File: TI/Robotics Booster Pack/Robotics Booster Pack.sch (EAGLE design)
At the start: 81 parts, among them U11 SCHA4B0400, U13 XBEE-1XBEE-1_LOCK, U14 TPS5450, U16 TPS62152.RGT, U3 DRV8800, U4 DRV8800, U5 DRV8800, U6 DRV8800, U7 PCA9557.RGV, U8 MPU-6050, U9 INA220.DGS

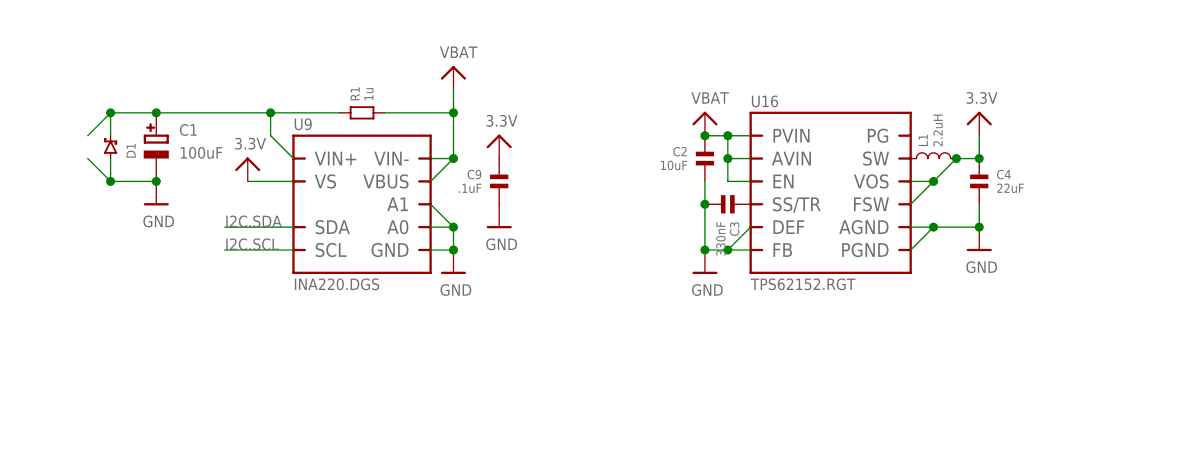
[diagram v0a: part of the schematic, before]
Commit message: Continued working on RBP v3 Using TPS62177 for 3.3v regulator circuit, new Vin headers, moving things around.
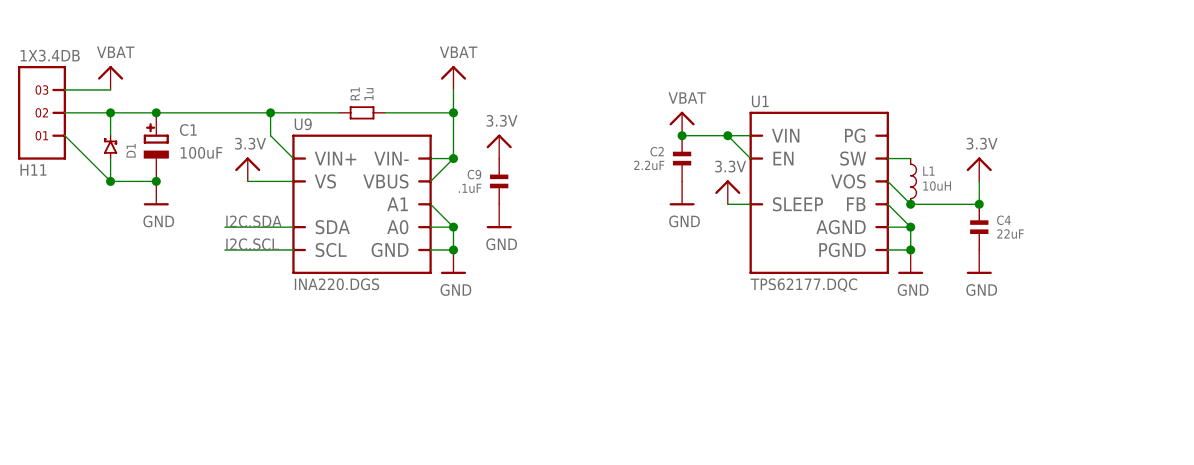
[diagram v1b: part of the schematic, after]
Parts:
- removed C3: 330nF, standardparts:CAPACITOR.0603
- removed U16: TPS62152.RGT, packages(ti):TPS6215X.RGT
- added H11: 1X3.4DB, te-connectivity:1X3.4DB
- added U1: TPS62177.DQC, packages(ti):TPS62177.DQC
- C2: value 10uF -> 2.2uF
- L1: value 2.2uH -> 10uH; device coilcraft:INDUCTOR.XAL4020 -> bourns:INDUCTOR-SRN6045
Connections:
- removed net N$23: C3.1, U16.SS/TR
- net 3.3V: now also U1.SLEEP, U1.VOS; no longer U16.FSW, U16.VOS
- net GND: now also H11.1, U1.AGND, U1.FB, U1.PGND; no longer C3.2, U16.AGND, U16.DEF, U16.FB, U16.PGND
- net N$1: now also U1.SW; no longer U16.SW
- net N$22: now also H11.2
- net VBAT: now also H11.3, U1.EN, U1.VIN; no longer U16.AVIN, U16.EN, U16.PVIN
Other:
- moved on the sheet: C2, C4, L1

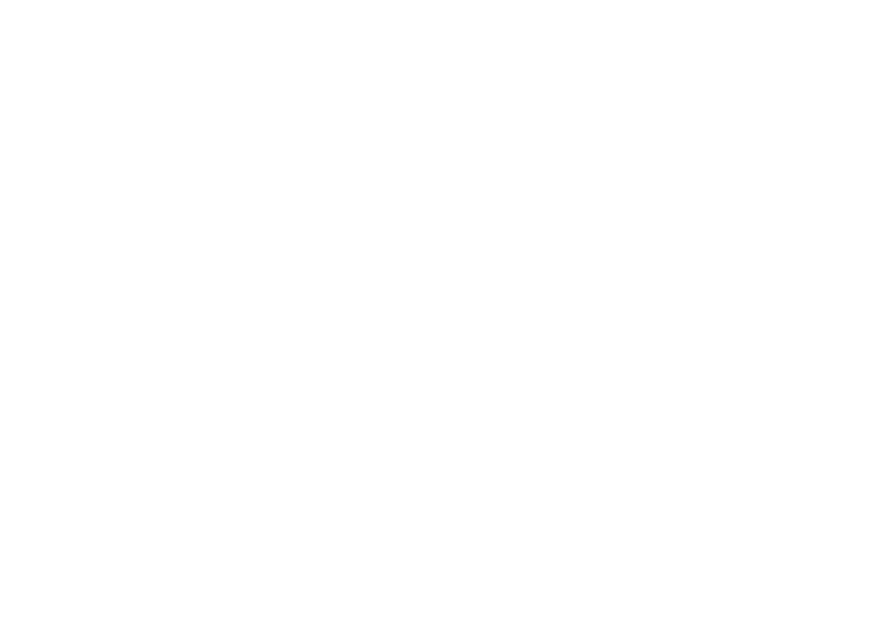
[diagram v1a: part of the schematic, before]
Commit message: COntinuing work on RBP v3 Added smd headers to replace Launchpad throguh hole headers (more routing space on the bottom) Moved around motor controllers -n- stuff.
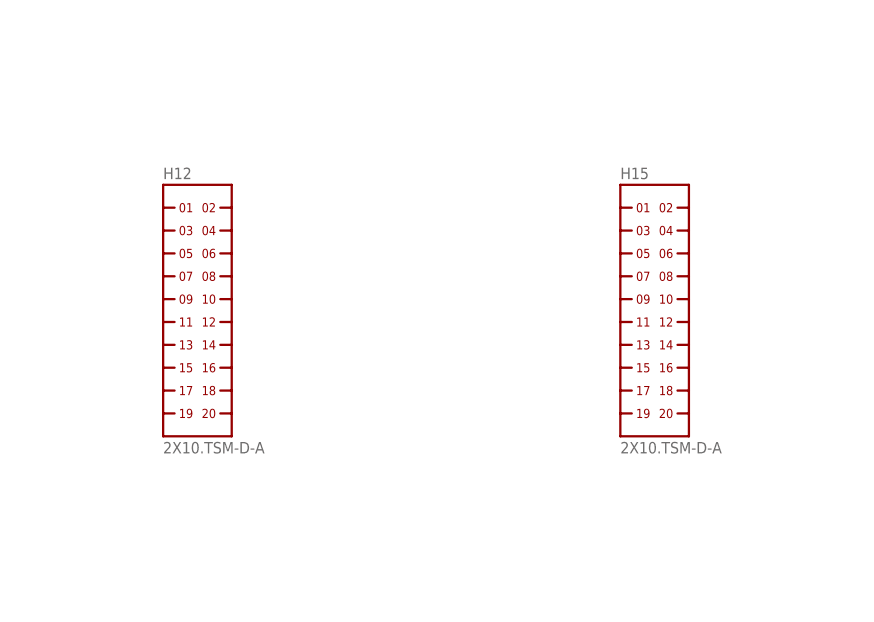
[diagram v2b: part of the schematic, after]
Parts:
- added H12, H15: 2X10.TSM-D-A, headers(.1in)(samtec):2X10.TSM-D-A
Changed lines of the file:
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@@
 <grid distance="0.1" unitdist="inch" unit="inch" style="lines" multiple="1" display="no" altdistance="0.01" altunitdist="inch" altunit="inch"/>
 <layers>
-<layer number="1" name="Top" color="4" fill="1" visible="yes" active="no"/>
-<layer number="2" name="Route2" color="1" fill="3" visible="yes" active="no"/>
-<layer number="3" name="Route3" color="4" fill="3" visible="yes" active="no"/>
-<layer number="4" name="Route4" color="1" fill="4" visible="yes" active="no"/>
-<layer number="5" name="Route5" color="4" fill="4" visible="yes" active="no"/>
-<layer number="6" name="Route6" color="1" fill="8" visible="yes" active="no"/>
-<layer number="7" name="Route7" color="4" fill="8" visible="yes" active="no"/>
-<layer number="8" name="Route8" color="1" fill="2" visible="yes" active="no"/>
-<layer number="9" name="Route9" color="4" fill="2" visible="yes" active="no"/>
-<layer number="10" name="Route10" color="1" fill="7" visible="yes" active="no"/>
-<layer number="11" name="Route11" color="4" fill="7" visible="yes" active="no"/>
-<layer number="12" name="Route12" color="1" fill="5" visible="yes" active="no"/>
-<layer number="13" name="Route13" color="4" fill="5" visible="yes" active="no"/>
-<layer number="14" name="Route14" color="1" fill="6" visible="yes" active="no"/>
-<layer number="15" name="Route15" color="4" fill="6" visible="yes" active="no"/>
-<layer number="16" name="Bottom" color="1" fill="1" visible="yes" active="no"/>
-<layer number="17" name="Pads" color="2" fill="1" visible="yes" active="no"/>
-<layer number="18" name="Vias" color="2" fill="1" visible="yes" active="no"/>
-<layer number="19" name="Unrouted" color="6" fill="1" visible="yes" active="no"/>
-<layer number="20" name="Dimension" color="15" fill="1" visible="yes" active="no"/>
-<layer number="21" name="tPlace" color="7" fill="1" visible="yes" active="no"/>
-<layer number="22" name="bPlace" color="7" fill="1" visible="yes" active="no"/>
-<layer number="23" name="tOrigins" color="15" fill="1" visible="yes" active="no"/>
-<layer number="24" name="bOrigins" color="15" fill="1" visible="yes" active="no"/>
-<layer number="25" name="tNames" color="7" fill="1" visible="yes" active="no"/>
-<layer number="26" name="bNames" color="7" fill="1" visible="yes" active="no"/>
-<layer number="27" name="tValues" color="7" fill="1" visible="yes" active="no"/>
-<layer number="28" name="bValues" color="7" fill="1" visible="yes" active="no"/>
+<layer number="1" name="Top" color="4" fill="1" visible="no" active="no"/>
+<layer number="2" name="Route2" color="1" fill="3" visible="no" active="no"/>
+<layer number="3" name="Route3" color="4" fill="3" visible="no" active="no"/>
+<layer number="4" name="Route4" color="1" fill="4" visible="no" active="no"/>
+<layer number="5" name="Route5" color="4" fill="4" visible="no" active="no"/>
+<layer number="6" name="Route6" color="1" fill="8" visible="no" active="no"/>
+<layer number="7" name="Route7" color="4" fill="8" visible="no" active="no"/>
+<layer number="8" name="Route8" color="1" fill="2" visible="no" active="no"/>
+<layer number="9" name="Route9" color="4" fill="2" visible="no" active="no"/>
+<layer number="10" name="Route10" color="1" fill="7" visible="no" active="no"/>
+<layer number="11" name="Route11" color="4" fill="7" visible="no" active="no"/>
+<layer number="12" name="Route12" color="1" fill="5" visible="no" active="no"/>
+<layer number="13" name="Route13" color="4" fill="5" visible="no" active="no"/>
+<layer number="14" name="Route14" color="1" fill="6" visible="no" active="no"/>
+<layer number="15" name="Route15" color="4" fill="6" visible="no" active="no"/>
+<layer number="16" name="Bottom" color="1" fill="1" visible="no" active="no"/>
+<layer number="17" name="Pads" color="2" fill="1" visible="no" active="no"/>
+<layer number="18" name="Vias" color="2" fill="1" visible="no" active="no"/>
+<layer number="19" name="Unrouted" color="6" fill="1" visible="no" active="no"/>
+<layer number="20" name="Dimension" color="15" fill="1" visible="no" active="no"/>
+<layer number="21" name="tPlace" color="7" fill="1" visible="no" active="no"/>
+<layer number="22" name="bPlace" color="7" fill="1" visible="no" active="no"/>
+<layer number="23" name="tOrigins" color="15" fill="1" visible="no" active="no"/>
+<layer number="24" name="bOrigins" color="15" fill="1" visible="no" active="no"/>
+<layer number="25" name="tNames" color="7" fill="1" visible="no" active="no"/>
+<layer number="26" name="bNames" color="7" fill="1" visible="no" active="no"/>
+<layer number="27" name="tValues" color="7" fill="1" visible="no" active="no"/>
+<layer number="28" name="bValues" color="7" fill="1" visible="no" active="no"/>
 <layer number="29" name="tStop" color="7" fill="3" visible="no" active="no"/>
 <layer number="30" name="bStop" color="7" fill="6" visible="no" active="no"/>
@@
 <layer number="35" name="tGlue" color="7" fill="4" visible="no" active="no"/>
 <layer number="36" name="bGlue" color="7" fill="5" visible="no" active="no"/>
-<layer number="37" name="tTest" color="7" fill="1" visible="yes" active="no"/>
-<layer number="38" name="bTest" color="7" fill="1" visible="yes" active="no"/>
+<layer number="37" name="tTest" color="7" fill="1" visible="no" active="no"/>
+<layer number="38" name="bTest" color="7" fill="1" visible="no" active="no"/>
 <layer number="39" name="tKeepout" color="4" fill="11" visible="no" active="no"/>
 <layer number="40" name="bKeepout" color="1" fill="11" visible="no" active="no"/>
@@
 <layer number="44" name="Drills" color="7" fill="1" visible="no" active="no"/>
 <layer number="45" name="Holes" color="7" fill="1" visible="no" active="no"/>
-<layer number="46" name="Milling" color="3" fill="1" visible="yes" active="no"/>
-<layer number="47" name="Measures" color="7" fill="1" visible="yes" active="no"/>
-<layer number="48" name="Document" color="7" fill="1" visible="yes" active="no"/>
-<layer number="49" name="Reference" color="7" fill="1" visible="yes" active="no"/>
-<layer number="50" name="dxf" color="7" fill="1" visible="yes" active="no"/>
-<layer number="51" name="tDocu" color="7" fill="1" visible="yes" active="no"/>
-<layer number="52" name="bDocu" color="7" fill="1" visible="yes" active="no"/>
-<layer number="53" name="tGND_GNDA" color="7" fill="9" visible="yes" active="no"/>
-<layer number="54" name="bGND_GNDA" color="1" fill="9" visible="yes" active="no"/>
-<layer number="56" name="wert" color="7" fill="1" visible="yes" active="no"/>
-<layer number="59" name="tCarbon" color="7" fill="1" visible="yes" active="no"/>
-<layer number="60" name="bCarbon" color="7" fill="1" visible="yes" active="no"/>
+<layer number="46" name="Milling" color="3" fill="1" visible="no" active="no"/>
+<layer number="47" name="Measures" color="7" fill="1" visible="no" active="no"/>
+<layer number="48" name="Document" color="7" fill="1" visible="no" active="no"/>
+<layer number="49" name="Reference" color="7" fill="1" visible="no" active="no"/>
+<layer number="50" name="dxf" color="7" fill="1" visible="no" active="no"/>
+<layer number="51" name="tDocu" color="7" fill="1" visible="no" active="no"/>
+<layer number="52" name="bDocu" color="7" fill="1" visible="no" active="no"/>
+<layer number="53" name="tGND_GNDA" color="7" fill="9" visible="no" active="no"/>
+<layer number="54" name="bGND_GNDA" color="1" fill="9" visible="no" active="no"/>
+<layer number="56" name="wert" color="7" fill="1" visible="no" active="no"/>
+<layer number="59" name="tCarbon" color="7" fill="1" visible="no" active="no"/>
+<layer number="60" name="bCarbon" color="7" fill="1" visible="no" active="no"/>
 <layer number="91" name="Nets" color="2" fill="1" visible="yes" active="yes"/>
 <layer number="92" name="Busses" color="1" fill="1" visible="yes" active="yes"/>
@@
 <part name="L1" library="bourns" deviceset="INDUCTOR" device="-SRN6045" value="10uH"/>
 <part name="U$15" library="microbuilder" deviceset="3.3V" device=""/>
+<part name="H12" library="headers(.1in)(samtec)" deviceset="2X10" device=".TSM-D-A"/>
+<part name="H15" library="headers(.1in)(samtec)" deviceset="2X10" device=".TSM-D-A"/>
 </parts>
 <sheets>
@@
 <instance part="L1" gate="G$1" x="104.14" y="231.14" rot="R270"/>
 <instance part="U$15" gate="G$1" x="83.82" y="231.14"/>
+<instance part="H12" gate="G$1" x="307.34" y="154.94"/>
+<instance part="H15" gate="G$1" x="358.14" y="154.94"/>
 </instances>
 <busses>

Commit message: Continuing RBP v3 rerouting. Figured out desired placement of headers. Thinking of adding FET to control power going out of board (NTMFS4897NFT1G). Need to replace IO expander; might need 16 pins instead of 8. Already running low on space...
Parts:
- removed C34: 100uF, microbuilder:CAP_ELECTROLYTICPANASONIC_D
- removed C39: 220uF, microbuilder:CAP_ELECTROLYTICPANASONIC_D
- removed H13, H14: 2X3, headers(.1in):2X3
- added H16, H17, H18, H19, H20, H21, H22, H23, H25, H26, H27, H28: 1X4, headers(.1in):1X4
- H1, H2, H3, H4, H5, H6: value 1X6 -> 1X4; device headers(.1in):1X6 -> headers(.1in):1X4
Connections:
- removed net VSERVO: C39.+, H2.1, H2.2, H2.3, H2.4, H2.5, H2.6
- new net N$12: H12.9
- new net N$15: H12.11
- new net N$16: H12.13
- new net N$17: H12.15
- new net N$2: H12.1
- new net N$23: H12.17
- new net N$26: H12.19
- new net N$28: H12.20
- new net N$3: H12.3
- new net N$30: H12.18
- new net N$31: H12.16
- new net N$32: H12.14
- new net N$36: H12.12
- new net N$41: H12.10
- new net N$42: H12.8
- new net N$43: H12.6
- new net N$44: H12.4
- new net N$45: H12.2
- new net N$46: H15.1
- new net N$47: H15.3
- new net N$48: H15.5
- new net N$49: H15.7
- new net N$50: H15.9
- new net N$51: H15.11
- new net N$52: H15.13
- new net N$53: H15.15
- new net N$54: H15.17
- new net N$55: H15.19
- new net N$56: H15.20
- new net N$57: H15.18
- new net N$58: H15.16
- new net N$59: H15.14
- new net N$6: H12.7
- new net N$60: H15.12
- new net N$61: H15.10
- new net N$62: H15.8
- new net N$63: H15.6
- new net N$64: H15.4
- new net N$65: H15.2
- new net N$66: H20.1, H20.2, H20.3, H20.4
- new net N$67: H23.1, H23.2, H23.3, H23.4
- new net N$68: H27.1, H27.2, H27.3, H27.4
- new net N$69: H2.1, H2.2, H2.3, H2.4
- new net N$70: H5.1, H5.2, H5.3, H5.4
- new net N$71: H17.1, H17.2, H17.3, H17.4
- net 3.3V: no longer H13.3, H14.3
- net AD0: no longer H6.1
- net AD1: no longer H6.2
- net AD2: no longer H6.3
- net AD3: no longer H6.4
- net AD4: no longer H6.5
- net AD5: no longer H6.6
- net GND: now also H11.3, H18.1, H18.2, H18.3, H18.4, H21.1, H21.2, H21.3, H21.4, H25.1, H25.2, H25.3, H25.4, H28.1, H28.2, H28.3, H28.4, H3.1, H3.2, H3.3, H3.4, H6.1, H6.2, H6.3, H6.4; no longer C34.-, C39.-, H1.1, H1.2, H1.3, H1.4, H1.5, H1.6, H11.1, H13.1, H14.1, H4.1, H4.2, H4.3, H4.4, H4.5, H4.6
- net N$4: now also H12.5; no longer C34.+, H5.1, H5.2, H5.3, H5.4, H5.5, H5.6
- net QEI0.A: no longer H13.5
- net QEI0.B: no longer H13.6
- net QEI1.A: no longer H14.5
- net QEI1.B: no longer H14.6
- net SVRO0: no longer H3.1
- net SVRO1: no longer H3.2
- net SVRO2: no longer H3.3
- net SVRO3: no longer H3.4
- net SVRO4: no longer H3.5
- net SVRO5: no longer H3.6
- net VBAT: now also H11.1; no longer H11.3
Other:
- note added: "TODO: - Move Launchpad pinouts to SMD headers - - Add UART1, I2C0, and SSI0 headers -"
- moved on the sheet: H11

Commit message: Got everything mostly figured out as to where I want things. Using larger capacitors. Pin header mappings decided on. Routing will be hell... Still need to figure out how to distribute all power variants (3.3, 5v, Vin) to all header blocks (3.3v for signals, 5v for signals/servos, Vin for servo overvolting)
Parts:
- removed C16, C18: 47uF, microbuilder:CAP_ELECTROLYTICPANASONIC_D
- removed C40: 330uF, microbuilder:CAP_ELECTROLYTICPANASONIC_D
- removed H21, H27, H28: 1X4, headers(.1in):1X4
- removed H24: 1X2, headers(.1in):1X2
- removed J3: (no value), solderjumper:SOLDERJUMPER.2.LRG
- removed J4: (no value), solderjumper:SOLDERJUMPER.3.LRG.23
- added C10, C11, C3, C8: (no value), adafruit:CPOL-USE
- added H30: 2X10.TSM-D-A, headers(.1in)(samtec):2X10.TSM-D-A
- added H31: 1X3.4DB, te-connectivity:1X3.4DB
- added J1, J2, J5: (no value), solderjumper:SOLDERJUMPER.2.LRG
- C1: value 100uF -> (none); device microbuilder:CAP_ELECTROLYTICPANASONIC_D -> adafruit:CPOL-USE
- H10, H8: value 1X4.182440000 -> 1X4; device weidmuller:1X4.182440000 -> headers(.1in):1X4
- H11: value 1X3.4DB -> 1X4; device te-connectivity:1X3.4DB -> headers(.1in):1X4
- H12, H15: value 2X10.TSM-D-A -> 1X4; device headers(.1in)(samtec):2X10.TSM-D-A -> headers(.1in):1X4
- H19, H20: value 1X4 -> 1X2; device headers(.1in):1X4 -> headers(.1in):1X2
- H25: value 1X4 -> 2X10.TSM-D-A; device headers(.1in):1X4 -> headers(.1in)(samtec):2X10.TSM-D-A
- H26: value 1X4 -> 1X8; device headers(.1in):1X4 -> weidmuller:1X8
- H7, H9: value 1X3 -> 1X4; device headers(.1in):1X3 -> headers(.1in):1X4
- renumbered H22 to H13, H23 to H14, U$3 to U$21
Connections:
- removed net N$12: H12.9
- removed net N$15: H12.11
- removed net N$16: H12.13
- removed net N$17: H12.15
- removed net N$2: H12.1
- removed net N$23: H12.17
- removed net N$26: H12.19
- removed net N$28: H12.20
- removed net N$3: H12.3
- removed net N$30: H12.18
- removed net N$31: H12.16
- removed net N$32: H12.14
- removed net N$36: H12.12
- removed net N$4: H12.5
- removed net N$41: H12.10
- removed net N$42: H12.8
- removed net N$43: H12.6
- removed net N$44: H12.4
- removed net N$45: H12.2
- removed net N$46: H15.1
- removed net N$47: H15.3
- removed net N$48: H15.5
- removed net N$49: H15.7
- removed net N$50: H15.9
- removed net N$51: H15.11
- removed net N$52: H15.13
- removed net N$53: H15.15
- removed net N$54: H15.17
- removed net N$55: H15.19
- removed net N$56: H15.20
- removed net N$57: H15.18
- removed net N$58: H15.16
- removed net N$59: H15.14
- removed net N$6: H12.7
- removed net N$60: H15.12
- removed net N$61: H15.10
- removed net N$62: H15.8
- removed net N$63: H15.6
- removed net N$64: H15.4
- removed net N$65: H15.2
- removed net N$68 (its old number): H27.1, H27.2, H27.3, H27.4
- removed net VDD: J4.2
- new net N$71: H8.1, H8.2, H8.3, H8.4
- new net N$72: C10.+, C28.1, C29.1, U5.VMOT, U6.VMOT
- new net N$73: C11.+, C30.1, C31.1, U3.VMOT, U4.VMOT
- new net PA2: H25.20, H7.1
- new net PA3: H25.18, H7.2
- new net PA4: H25.16, H7.3
- new net PA5: H30.15, H7.4
- new net PA6: H30.17, H4.3
- new net PA7: H30.19, H4.4
- new net PB0: H30.5
- new net PB1: H30.7
- new net PB2: H25.4
- new net PB3: H25.5
- new net PB4: H10.3, H30.13
- new net PB5: H10.4, H30.3
- new net PB6: H10.1, H25.14
- new net PB7: H10.2, H25.12
- new net PC4: H25.7
- new net PC5: H16.3, H25.9
- new net PC6: H16.4, H25.11
- new net PC7: H25.13
- new net PD0: H13.3, H30.6
- new net PD1: H13.4, H30.8
- new net PD2: H30.10, H4.2
- new net PD3: H30.12, H4.1
- new net PD6: H16.1, H25.15
- new net PD7: H16.2, H25.17
- new net PE0: H1.4, H25.6
- new net PE1: H1.3, H30.14
- new net PE2: H1.2, H30.16
- new net PE3: H1.1, H30.18
- new net PE4: H13.1, H30.9
- new net PE5: H13.2, H30.11
- new net PF0: H25.8
- new net PF1: H30.20
- new net PF2: H25.1
- new net PF3: H25.3
- new net PF4: H25.19
- net !RST: now also H25.10; no longer H24.1
- net 3.3V: now also H30.1
- net 5.0V: now also C8.+, H30.2; no longer C40.+, J4.3
- net FET0.D: now also H20.1; no longer H9.1
- net FET1.D: now also H20.2; no longer H9.3
- net GND: now also C10.-, C11.-, C8.-, H12.1, H12.2, H12.3, H12.4, H15.1, H15.2, H15.3, H15.4, H30.4, H31.3, H9.1, H9.3, H9.4; no longer C16.-, C18.-, C40.-, H11.3, H21.1, H21.2, H21.3, H21.4, H24.2, H25.1, H25.3, H25.4, H28.1, H28.2, H28.3, H28.4
- net M0+: now also H26.1; no longer H8.1
- net M0-: now also H26.2; no longer H8.2
- net M1+: now also H26.3; no longer H8.3
- net M1-: now also H26.4; no longer H8.4
- net M2+: now also H26.5; no longer H10.1
- net M2-: now also H26.6; no longer H10.2
- net M3+: now also H26.7; no longer H10.3
- net M3-: now also H26.8; no longer H10.4
- net N$22: now also H31.2; no longer H11.2
- net N$66: now also H11.1, H11.2, H11.3, H11.4; no longer H20.1, H20.2, H20.3, H20.4
- net VBAT: now also H31.1; no longer C16.+, C18.+, C28.1, C29.1, C30.1, C31.1, H11.1, J3.2, J4.1, U3.VMOT, U4.VMOT, U5.VMOT, U6.VMOT
- net VFET: now also H19.1, H19.2; no longer H7.1, H7.2, H7.3, J3.1
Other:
- note added: "TODO: - Apply Pin Map to signal names - Add UART1 and I2C0 headers - Finish deciding on final layout of board - Figure out how to map power to headers"
- note removed: "TODO: - Move Launchpad pinouts to SMD headers - - Add UART1, I2C0, and SSI0 headers -"
- moved on the sheet: D3, D4, H10, H16, H17, H18, H8, Q1.A, Q1.B
